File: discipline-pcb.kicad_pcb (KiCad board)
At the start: 2 copper layers, 304.9 x 122.8 mm, 197 parts, among them J1 AVR-ISP-6, SW1 KEYSW, SW10 KEYSW, SW11 KEYSW, SW12 KEYSW, SW13 KEYSW, SW14 KEYSW, SW15 KEYSW, SW16 KEYSW, SW17 KEYSW, SW18 KEYSW, SW19 KEYSW, SW2 KEYSW, SW20 KEYSW, SW21 KEYSW, SW22 KEYSW, SW23 KEYSW, SW24 KEYSW, SW25 KEYSW, SW26 KEYSW, SW27 KEYSW, SW28 KEYSW, SW29 KEYSW, SW3 KEYSW, SW30 KEYSW, SW31 KEYSW, SW32 KEYSW, SW33 KEYSW, SW34 KEYSW, SW35 KEYSW, SW36 KEYSW, SW37 KEYSW, SW38 KEYSW, SW39 KEYSW, SW4 KEYSW, SW40 KEYSW, SW41 KEYSW, SW42 KEYSW, SW43 KEYSW, SW44 KEYSW, SW45 KEYSW, SW46 KEYSW, SW47 KEYSW, SW48 KEYSW, SW49 KEYSW, SW5 KEYSW, SW50 KEYSW, SW51 KEYSW, SW52 KEYSW, SW53 KEYSW, SW54 KEYSW, SW55 KEYSW, SW56 KEYSW, SW57 KEYSW, SW58 KEYSW, SW59 KEYSW, SW6 KEYSW, SW60 KEYSW, SW61 KEYSW, SW62 KEYSW, SW63 KEYSW, SW64 KEYSW, SW65 KEYSW, SW66 KEYSW, SW67 KEYSW, SW68 KEYSW, SW69 KEYSW, SW7 KEYSW, SW70 KEYSW, SW71 KEYSW, SW72 KEYSW, SW73 KEYSW, SW74 KEYSW, SW75 KEYSW, SW76 KEYSW, SW77 KEYSW, SW78 KEYSW, SW8 KEYSW, SW9 KEYSW, U1 ATmega32A-PU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

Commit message: modified schematic and footprints for my layout. still need to rearrange traces
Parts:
- removed the D71 at (96.7, 147.0)
- removed the G*** at (155.1, 168.3) (x2)
- removed the G*** at (155.2, 163.6) (x2)
- removed the G*** at (155.1, 174.0) (x2)
- removed the REF** at (184.8, 171.0)
- removed ST72: 7U, cftkb:MX-7U-Stabilizer
- removed the SW68 at (294.5, 165.9)
- removed the SW69 at (68.3, 127.8)
- removed SW74: KEYSW, cftkb:SW_Cherry_MX1A_1.50u_PCBNOSCREEN
- removed SW75, SW77: KEYSW, cftkb:SW_Cherry_MX1A_1.00u_PCB-NOSCREEN
- removed SW76: KEYSW, cftkb:SW_Cherry_MX1A_ISOEnter_PCB_ReversedStabilizer
- removed SW78: KEYSW, cftkb:SW_Cherry_MX1A_1.25u_PCBNOSCREEN
- added D15: , cftkb:D_DO-35_SOD27_P5.08mm_Horizontal, F.Cu at (200.7, 50.8)
- added D62: , cftkb:D_DO-35_SOD27_P5.08mm_Horizontal, F.Cu at (186.6, 50.6)
- added D64: , cftkb:D_DO-35_SOD27_P5.08mm_Horizontal, F.Cu at (199.8, 44.0)
- added SW62: KEYSW-keyboard_parts, cftkb:SW_Cherry_MX_2.75u_PCB_nosilk_flippedstabs, F.Cu at (154.0, 165.9)
- added SW64: KEYSW-keyboard_parts, cftkb:SW_Cherry_MX_2.25u_PCB_nosilk_fliippedstabs, F.Cu at (225.3, 165.9)
- SW15: value KEYSW -> Rotary_Encoder_Switch; footprint cftkb:SW_Cherry_MX1A_1.00u_PCB-NOSCREEN -> cftkb:RotaryEncoder_Alps_EC11E-Switch_Vertical_H20mm_nosilk
- SW43, SW45: footprint cftkb:SW_Cherry_MX1A_2.25u_PCBNOSCREEN -> cftkb:SW_Cherry_MX_2.25u_PCB_nosilk_fliippedstabs
- SW63: renamed from SW62; footprint cftkb:SW_Cherry_MX1A_1.00u_PCB-NOSCREEN -> cftkb:SW_Cherry_MX1A_1.25u_PCBNOSCREEN
- SW70: value KEYSW -> KEYSW-keyboard_parts; footprint cftkb:SW_Cherry_MX1A_1.50u_PCBNOSCREEN -> cftkb:SW_Cherry_MX_2.25u_PCB_nosilk_fliippedstabs
- SW71: value KEYSW -> KEYSW-keyboard_parts; footprint cftkb:SW_Cherry_MX1A_1.50u_PCBNOSCREEN -> cftkb:SW_Cherry_MX1A_1.25u_PCBNOSCREEN
- SW72: value KEYSW -> KEYSW-keyboard_parts; footprint cftkb:SW_Cherry_MX1A_1.00u_PCB-NOSCREEN -> cftkb:SW_Cherry_MX_2.75u_PCB_nosilk_flippedstabs
- SW73: value KEYSW -> KEYSW-keyboard_parts; footprint cftkb:SW_Cherry_MX1A_1.50u_PCBNOSCREEN -> cftkb:SW_Cherry_MX_6.25u_PCB_nosilk_flippedstabs
- moved G*** 125.9 mm to (280.4, 176.4)
- moved G*** 99.9 mm to (255.0, 174.0)
- moved SW71 83.3 mm to (182.5, 165.9)
- moved G*** 81.3 mm to (236.5, 176.8)
- moved SW70 78.6 mm to (149.2, 165.9)
- moved SW73 73.9 mm to (187.3, 165.9)
- moved SW72 40.4 mm to (220.7, 165.9)
- moved SW66 26.4 mm to (282.8, 165.9)
- moved SW65 16.7 mm to (258.8, 165.9)
- moved REF** 8.76 mm to (199.3, 161.5)
- moved SW15 5.67 mm to (349.1, 94.7)
- moved SW63 4.67 mm to (192.0, 165.9)
- renumbered D62 to D63, D64 to D65, D63 to D66, D65 to D67, D66 to D68, D67 to D69, D69 to D70, D70 to D71, SW64 to SW65, SW63 to SW66, SW65 to SW67, SW66 to SW68, SW67 to SW69
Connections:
- D63 pad 2: Net-(D62-Pad2) -> Net-(D63-Pad2)
- D66 pad 2: Net-(D63-Pad2) -> Net-(D66-Pad2)
- D68 pad 2: Net-(D66-Pad2) -> Net-(D68-Pad2)
- SW63 pad 2: Net-(D62-Pad2) -> Net-(D63-Pad2)
- SW66 pad 1: col9 -> col11
- SW66 pad 2: Net-(D63-Pad2) -> Net-(D66-Pad2)
- SW68 pad 2: Net-(D66-Pad2) -> Net-(D68-Pad2)
- SW70 pad 1: col0 -> col4
- SW70 pad 2: Net-(D59-Pad2) -> Net-(D62-Pad2)
- SW71 pad 1: col2 -> col6
- SW71 pad 2: Net-(D61-Pad2) -> Net-(D63-Pad2)
- SW72 pad 1: col6 -> col8
- SW72 pad 2: Net-(D62-Pad2) -> Net-(D64-Pad2)
- SW73 pad 1: col9 -> col6
- U1 pad 33: Net-(U1-Pad33) -> encB
- U1 pad 34: Net-(U1-Pad34) -> encA
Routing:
- net Net-(D62-Pad2): track 355.8 -> 0.00 mm
- net Net-(D68-Pad2): track 232.5 -> 423.1 mm
- net Net-(D66-Pad2): track 190.5 -> 279.4 mm
- net Net-(D63-Pad2): track 279.4 -> 355.8 mm
- net GND: vias 48 -> 46
- net (no net): vias 0 -> 2
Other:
- board text added: "kenneth seneres 2021"
- board text removed: "1.25U"
- board text removed: "1.25U ISO"
- board text removed: "1.5U"
- board text removed: "1U"
- board text removed: "1U ISO"
- board text removed: "2.25U ANSI"
- board text removed: "ANSI ENTER"
- board text removed: "ISO"
- board text removed: "ISO ENTER"
- board text removed: "STANDARD"
- board text removed: "STEPPED"

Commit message: little footprint changes in schematic
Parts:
- removed the D15 at (275.5, 71.2)
- removed G***: LOGO, logos:DISCIPLINE_SMALL_COPPER
- removed G***: LOGO, logos:rev1-1_16mm_copper
- removed G***: LOGO, logos:rev1-1_16mm_mask
- removed G***: LOGO, logos:coseyfannitutti_rev1_16mm_copper
- removed G***: LOGO, logos:coseyfannitutti_16mm
- removed G***: LOGO, logos:DISCIPLINE_SMALL_MASK
- removed G*** (x2): LOGO, logos:TOPY 4MM MASK
- removed REF** (x12): MountingHole_2.2mm_M2_Pad, MountingHole:MountingHole_2.2mm_M2_Pad
- SW43, SW45: footprint cftkb:SW_Cherry_MX_2.25u_PCB_nosilk_fliippedstabs -> cftkb:SW_Cherry_MX1A_2.25u_PCBNOSCREEN

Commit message: traces for matrix columns done
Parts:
- added D15: , cftkb:D_DO-35_SOD27_P5.08mm_Horizontal, F.Cu at (275.5, 71.2)
- added G***: LOGO, logos:rev1-1_16mm_mask, B.Cu at (236.5, 176.8)
- added G***: LOGO, logos:coseyfannitutti_16mm, B.Cu at (255.0, 174.0)
- added G***: LOGO, logos:DISCIPLINE_SMALL_MASK, B.Cu at (280.4, 176.4)
- added G***: LOGO, logos:TOPY 4MM MASK, F.Cu at (354.1, 71.1)
- added G***: LOGO, logos:TOPY 4MM MASK, F.Cu at (58.5, 71.1)
- added REF**: MountingHole_2.2mm_M2_Pad, MountingHole:MountingHole_2.2mm_M2_Pad, F.Cu at (206.2, 61.7)
- added REF**: MountingHole_2.2mm_M2_Pad, MountingHole:MountingHole_2.2mm_M2_Pad, F.Cu at (354.7, 61.7)
- added REF**: MountingHole_2.2mm_M2_Pad, MountingHole:MountingHole_2.2mm_M2_Pad, F.Cu at (57.8, 61.7)
- added REF**: MountingHole_2.2mm_M2_Pad, MountingHole:MountingHole_2.2mm_M2_Pad, F.Cu at (57.8, 80.4)
- added REF**: MountingHole_2.2mm_M2_Pad, MountingHole:MountingHole_2.2mm_M2_Pad, F.Cu at (206.2, 80.4)
- added REF**: MountingHole_2.2mm_M2_Pad, MountingHole:MountingHole_2.2mm_M2_Pad, F.Cu at (199.3, 161.5)
- added REF**: MountingHole_2.2mm_M2_Pad, MountingHole:MountingHole_2.2mm_M2_Pad, F.Cu at (206.2, 104.3)
- added REF**: MountingHole_2.2mm_M2_Pad, MountingHole:MountingHole_2.2mm_M2_Pad, F.Cu at (298.7, 104.3)
- added REF**: MountingHole_2.2mm_M2_Pad, MountingHole:MountingHole_2.2mm_M2_Pad, F.Cu at (113.8, 104.3)
- added REF**: MountingHole_2.2mm_M2_Pad, MountingHole:MountingHole_2.2mm_M2_Pad, F.Cu at (315.9, 161.1)
- added REF**: MountingHole_2.2mm_M2_Pad, MountingHole:MountingHole_2.2mm_M2_Pad, F.Cu at (96.6, 161.1)
- added REF**: MountingHole_2.2mm_M2_Pad, MountingHole:MountingHole_2.2mm_M2_Pad, F.Cu at (354.7, 80.4)
- SW62, SW64, SW70, SW71, SW72, SW73: value KEYSW-keyboard_parts -> KEYSW
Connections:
- U1 pad 14: Net-(U1-Pad14) -> encA
- U1 pad 15: Net-(U1-Pad15) -> encB
- U1 pad 33: encB -> Net-(U1-Pad33)
- U1 pad 34: encA -> Net-(U1-Pad34)
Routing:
- net col9: track 258.3 -> 220.7 mm
- net col10: track 249.2 -> 220.7 mm
- net col4: track 261.3 -> 286.1 mm
- net col8: track 244.5 -> 265.6 mm
- net Net-(D61-Pad2): track 425.1 -> 408.5 mm
- net col2: track 331.4 -> 318.7 mm
- net col11: track 212.1 -> 200.2 mm
- net Net-(D43-Pad2): track 153.6 -> 141.7 mm
- net Net-(D29-Pad2): track 127.9 -> 117.7 mm
- net col0: track 364.4 -> 354.3 mm
- net Net-(D63-Pad2): track 355.8 -> 348.6 mm
- net col12: track 184.1 -> 178.3 mm
- net col7: track 268.1 -> 262.6 mm
- net col13: track 161.3 -> 156.3 mm
- net col5: track 269.8 -> 266.6 mm
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
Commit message: pre drc
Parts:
- removed the D59 at (259.8, 69.5)
- removed the D68 at (247.2, 69.5)
- moved D59 169.1 mm to (77.7, 166.9), turned to 270 degrees
- moved D62 72.3 mm to (256.8, 67.8), turned to 270 degrees
- moved D64 57.5 mm to (250.4, 71.1), turned to 270 degrees
- moved D65 22.1 mm to (247.3, 69.6)
- moved D67 19.1 mm to (225.3, 71.1)
- moved D66 7.08 mm to (244.1, 67.8)
- moved D61 3.65 mm to (259.8, 69.6)
- renumbered D15 to D59
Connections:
- D59 pad 1: row0 -> row4
- D59 pad 2: Net-(D15-Pad2) -> Net-(D59-Pad2)
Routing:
- net Net-(D59-Pad2): track 459.8 -> 20.7 mm
- net Net-(D62-Pad2): track 0.00 -> 376.0 mm
- net Net-(D64-Pad2): track 0.00 -> 305.7 mm
- net Net-(D68-Pad2): track 423.1 -> 187.2 mm
- net Net-(D65-Pad2): track 188.7 -> 395.5 mm
- net row4: track 299.4 -> 429.8 mm
- net row3: track 404.8 -> 292.2 mm, vias 7 -> 5
- net Net-(D66-Pad2): track 279.4 -> 332.6 mm
- net Net-(D67-Pad2): track 215.1 -> 165.2 mm
- net Net-(D71-Pad2): track 15.0 -> 0.00 mm
- net col13: track 156.3 -> 144.4 mm
- net Net-(D45-Pad2): track 85.1 -> 75.6 mm
- net Net-(D61-Pad2): track 408.5 -> 401.0 mm
- net Net-(D15-Pad2): track 78.0 -> 84.1 mm
- net Net-(D31-Pad2): track 69.7 -> 65.0 mm
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
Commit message: pcb done
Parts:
- added G***: LOGO, cftkb:rev1-1_16mm_copper, B.Cu at (236.5, 176.8)
- added G***: LOGO, cftkb:coseyfannitutti_16mm_copper, B.Cu at (255.0, 174.0)
- added G***: LOGO, cftkb:DISCIPLINE_SMALL_COPPER, B.Cu at (280.4, 176.4)
- moved REF** 3.66 mm to (99.1, 163.8)
- moved REF** 3.03 mm to (318.0, 159.0)
- moved REF** 2.58 mm to (198.9, 164.1)
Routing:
- net encA: track 0.00 -> 30.5 mm, vias 0 -> 1
- net encB: track 0.00 -> 23.5 mm, vias 0 -> 1
- net Net-(D69-Pad2): track 159.7 -> 161.0 mm
- net Net-(D56-Pad2): track 146.5 -> 145.3 mm
- net Net-(D67-Pad2): track 165.2 -> 163.9 mm
- net Net-(D57-Pad2): track 152.2 -> 151.2 mm
- net Net-(D43-Pad2): track 141.7 -> 141.1 mm
- net Net-(D63-Pad2): track 350.0 -> 349.4 mm
- net GND: vias 33 -> 38
- net (no net): vias 1 -> 0
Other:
- board text added: "7/2/2019 - updated 7/18/2021"
- board text removed: "7/2/2019 - updated 12/3/2019"

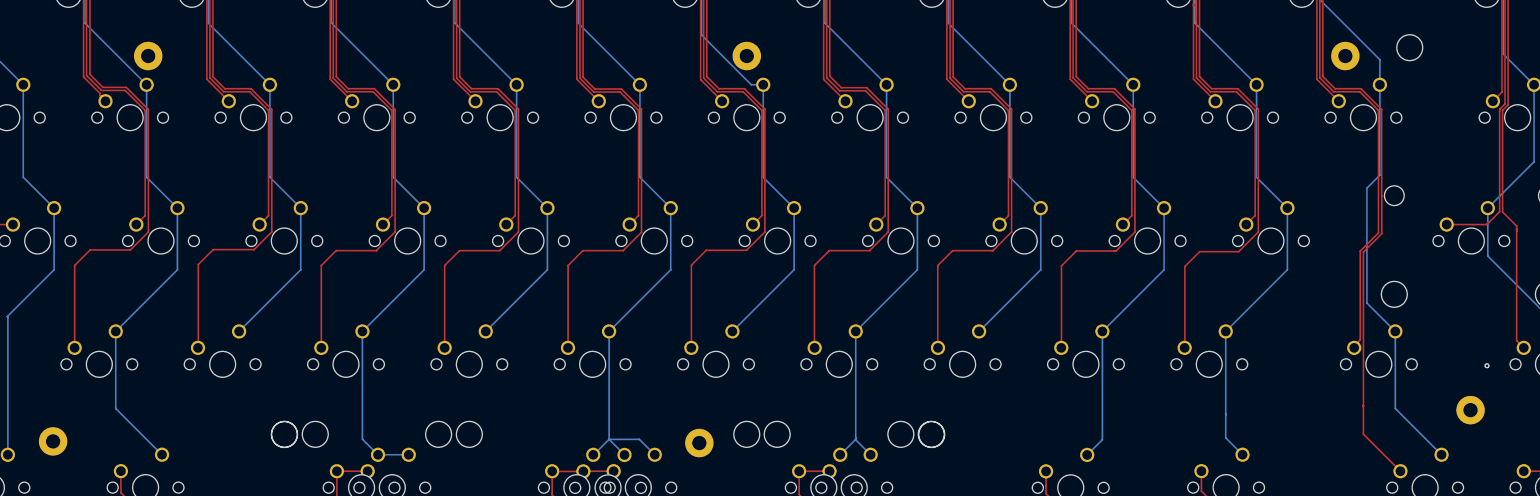
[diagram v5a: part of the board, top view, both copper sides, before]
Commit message: moved mounting holes
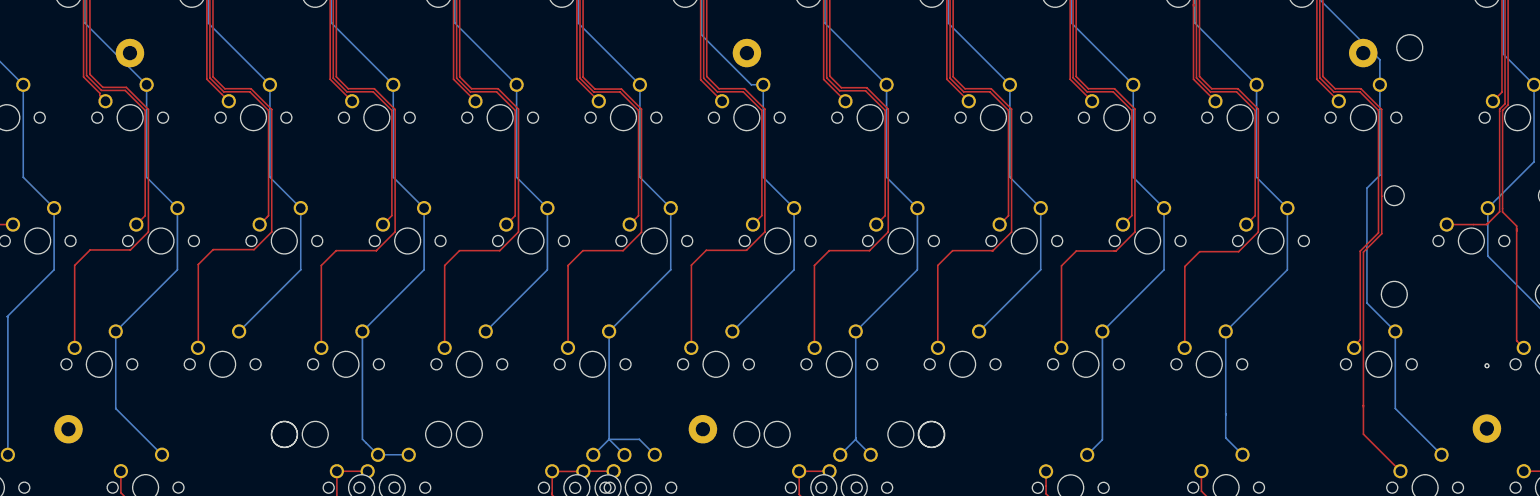
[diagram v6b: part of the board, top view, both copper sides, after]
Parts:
- moved REF** 3.81 mm to (320.5, 161.8)
- moved REF** 3.03 mm to (101.4, 161.9)
- moved REF** 2.86 mm to (110.9, 103.8)
- moved REF** 2.80 mm to (301.4, 103.8)
- moved REF** 2.21 mm to (199.4, 161.9)
- moved REF** 0.46 mm to (206.2, 103.8)

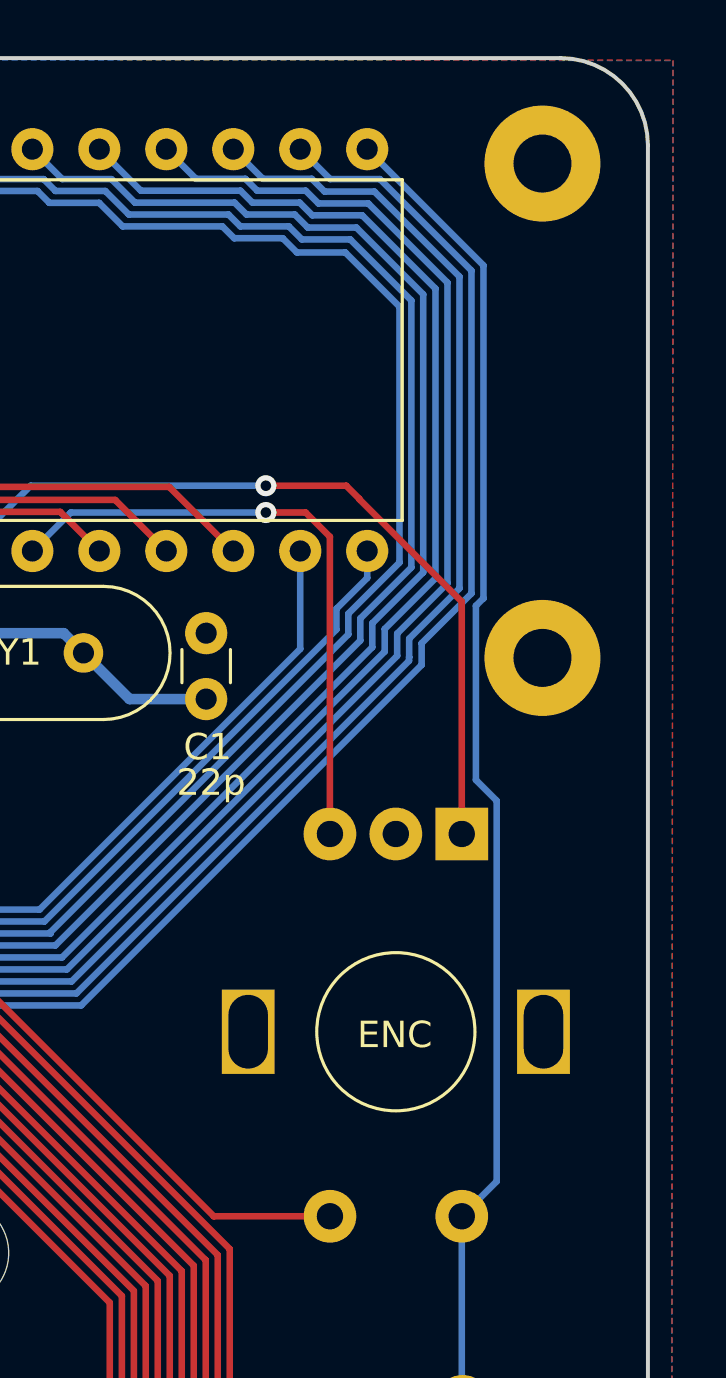
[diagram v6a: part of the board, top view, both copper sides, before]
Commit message: turned the rotary encoder slot into a switch/encoder combo slot
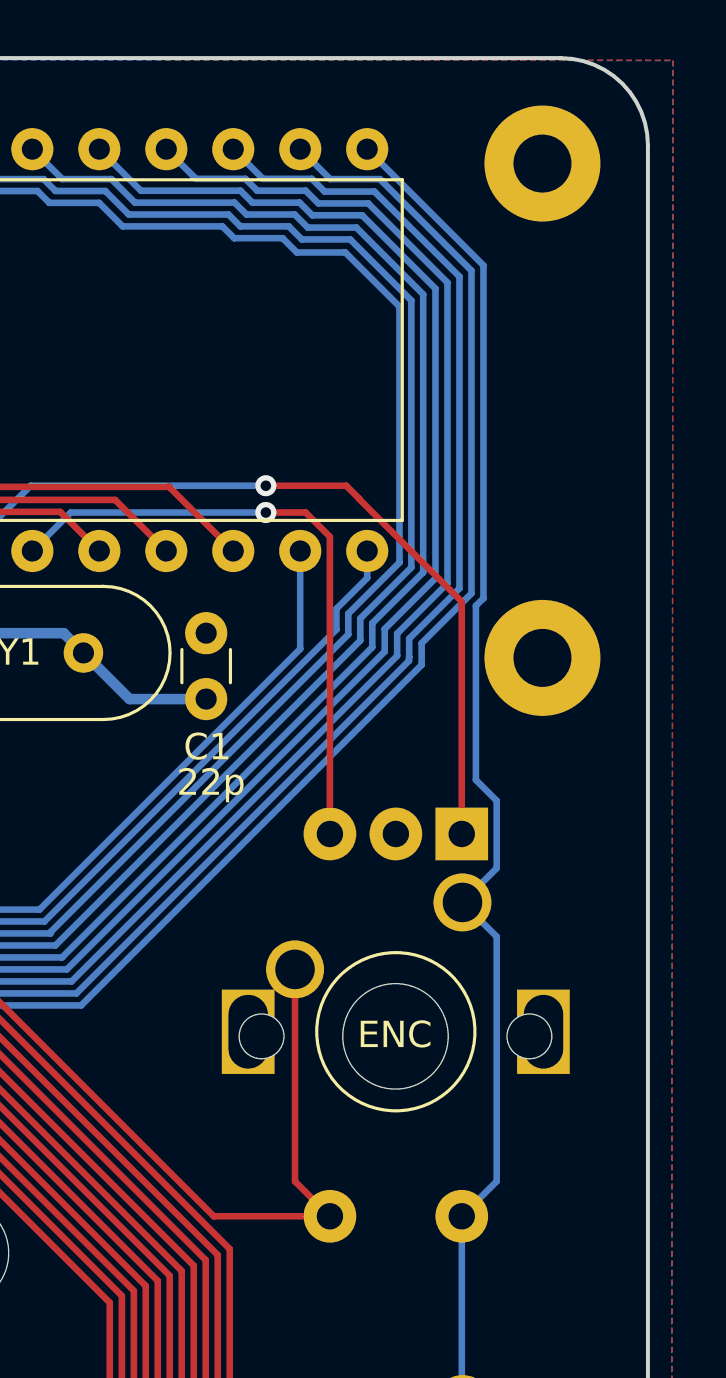
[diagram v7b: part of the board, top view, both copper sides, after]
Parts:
- added SW74: KEYSW, cftkb:SW_Cherry_MX1A_1.00u_PCB-NOSCREEN, F.Cu at (351.6, 89.7)
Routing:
- net Net-(D15-Pad2): track 84.1 -> 94.0 mm
- net col14: track 107.6 -> 108.7 mm

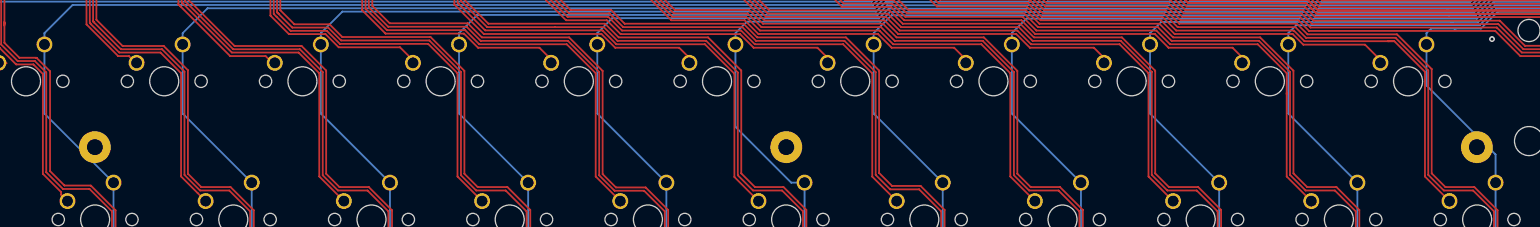
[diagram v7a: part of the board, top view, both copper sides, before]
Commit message: almost sent a pcb with a hole through a trace there
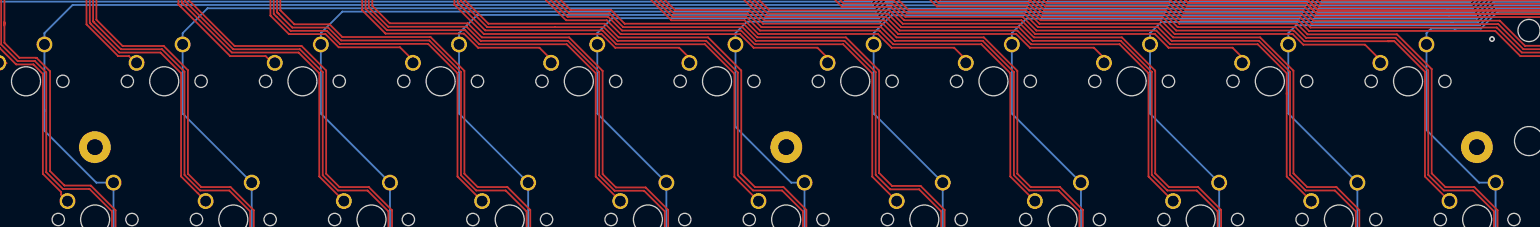
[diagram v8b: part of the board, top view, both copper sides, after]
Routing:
- net col2: track 318.7 -> 320.1 mm
- net col12: track 178.3 -> 179.6 mm
